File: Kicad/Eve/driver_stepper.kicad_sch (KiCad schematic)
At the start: 16 parts

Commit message: Kicad changes
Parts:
- removed C201, C202, C209: 0603/100nF/50V, symbol Device:C_Small
- removed C203, C204, C205, C207: 150µF/80V/45 mOhm, symbol Device:C_Polarized
- removed C206, C208, C210: 0603/100nF/16V, symbol Device:C_Small
- removed D201: SMBJ54A, symbol Device:D_Schottky
- removed Q? (x4): SQJ504EP-T1_GE3, SQJ968EPT1GE3, symbol SQJ504EP-T1_GE3:SQJ504EP-T1_GE3
- removed U?: TMC2590-TA, TQFP32_7X7_TRI, symbol TMC2590:TMC2590-TA
- added C? (x3): 0603/100nF/50V, symbol Device:C_Small
- added C? (x4): 150µF/80V/45 mOhm, symbol Device:C_Polarized
- added C? (x3): 0603/100nF/16V, symbol Device:C_Small
- added D?: SMBJ54A, symbol Device:D_Schottky
- added J? (x2): Conn_01x03, symbol Connector_Generic:Conn_01x03
- added Q? (x4): SQJ504EP-T1_GE3, SQJ968EPT1GE3, symbol SQJ504EP-T1_GE3:SQJ504EP-T1_GE3
- added R? (x2): 10, symbol Device:R
- added R? (x2): 0.075/2W, symbol Device:R
- added U?: TMC2590-TA, TQFP32_7X7_TRI, symbol TMC2590:TMC2590-TA
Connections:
- net 5VOUT: now also C?.2, U?.9 (5VOUT)
- net A1: now also Q?.5 (D1), Q?.6 (D2), U?.5 (BMA1)
- net A2: now also Q?.5 (D1), Q?.6 (D2), U?.4 (BMA2)
- net B1: now also Q?.5 (D1), Q?.6 (D2), U?.20 (BMB1)
- net B2: now also Q?.5 (D1), Q?.6 (D2), U?.21 (BMB2)
- net CLK: now also U?.16 (CLK)
- net CSN: now also U?.14 (CSN)
- net DIR: now also J?.2 (Pin_2), U?.30 (DIR)
- net ENN: now also U?.15 (ENN)
- net GND: now also C?.1, C?.1, C?.2, C?.2, C?.2, C?.2, C?.2, C?.2, C?.2, D?.2 (A), R?.2, R?.2, U?.1 (GND), U?.13 (SRBL), U?.28 (SRAL), U?.32 (TST_MODE), U?.33 (GND)
- net HA1: now also Q?.4 (G2), U?.2 (HA1)
- net HA2: now also Q?.4 (G2), U?.3 (HA2)
- net HB1: now also Q?.4 (G2), U?.23 (HB1)
- net HB2: now also Q?.4 (G2), U?.22 (HB2)
- net LA1: now also Q?.2 (G1), U?.6 (LA1)
- net LA2: now also Q?.2 (G1), U?.7 (LA2)
- net LB1: now also Q?.2 (G1), U?.19 (LB1)
- net LB2: now also Q?.2 (G1), U?.18 (LB2)
- net MISO: now also U?.10 (SDO)
- net MOSI: now also U?.11 (SDI)
- net SCK: now also U?.12 (SCK)
- net SG_TST: now also U?.27 (SG_TST)
- net SRA: now also R?.2, U?.8 (SRA)
- net SRB: now also R?.2, U?.17 (SRB)
- net STANDALONE_MODE: now also U?.26 (ST_ALONE)
- net STEP: now also J?.2 (Pin_2), U?.31 (STEP)
- net VCC_IO: now also C?.1, U?.29 (VCC_IO)
- net VHS: now also C?.2, U?.24 (VHS)
- new net: Q?.1 (S1), Q?.1 (S1), R?.1, R?.1 (x2)
- new net CON_DIR: J?.3 (Pin_3)
- new net CON_STEP: J?.3 (Pin_3)
- new net EXT_DIR: J?.1 (Pin_1)
- new net EXT_STEP: J?.1 (Pin_1)
- new net Vdc: C?.1, C?.1, C?.1, C?.1, C?.1, C?.1, C?.1, C?.2, D?.1 (K), Q?.3 (S2), Q?.3 (S2), Q?.3 (S2), Q?.3 (S2), U?.25 (VS)

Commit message: updtated Kicad ver 7.11.23
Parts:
- removed J? (x2): Conn_01x03, symbol Connector_Generic:Conn_01x03
- removed Q?: SQJ504EP-T1_GE3, SQJ968EPT1GE3, symbol SQJ504EP-T1_GE3:SQJ504EP-T1_GE3
- added J8: Conn_01x04, symbol Connector_Generic:Conn_01x04
- added Q1: SQJ504EP-T1_GE3, SQJ968EPT1GE3, symbol SQJ504EP-T1_GE3:SQJ504EP-T1_GE3
- C28: renamed from C?; value 150µF/80V/45 mOhm -> 150u; Vmax (none) -> 80
- gave numbers to parts that had none: 18
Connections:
- net A1: now also J8.3 (Pin_3), Q1.5 (D1), Q1.6 (D2)
- net A2: now also J8.4 (Pin_4)
- net B1: now also J8.1 (Pin_1)
- net B2: now also J8.2 (Pin_2)
- net HA1: now also Q1.4 (G2)
- net LA1: now also Q1.2 (G1)
- net Vdc: now also Q1.3 (S2)
- net at Q7.1 (S1), R24.1, R26.1: now also Q1.1 (S1)
- net MISO renamed SDO
- net MOSI renamed SDI

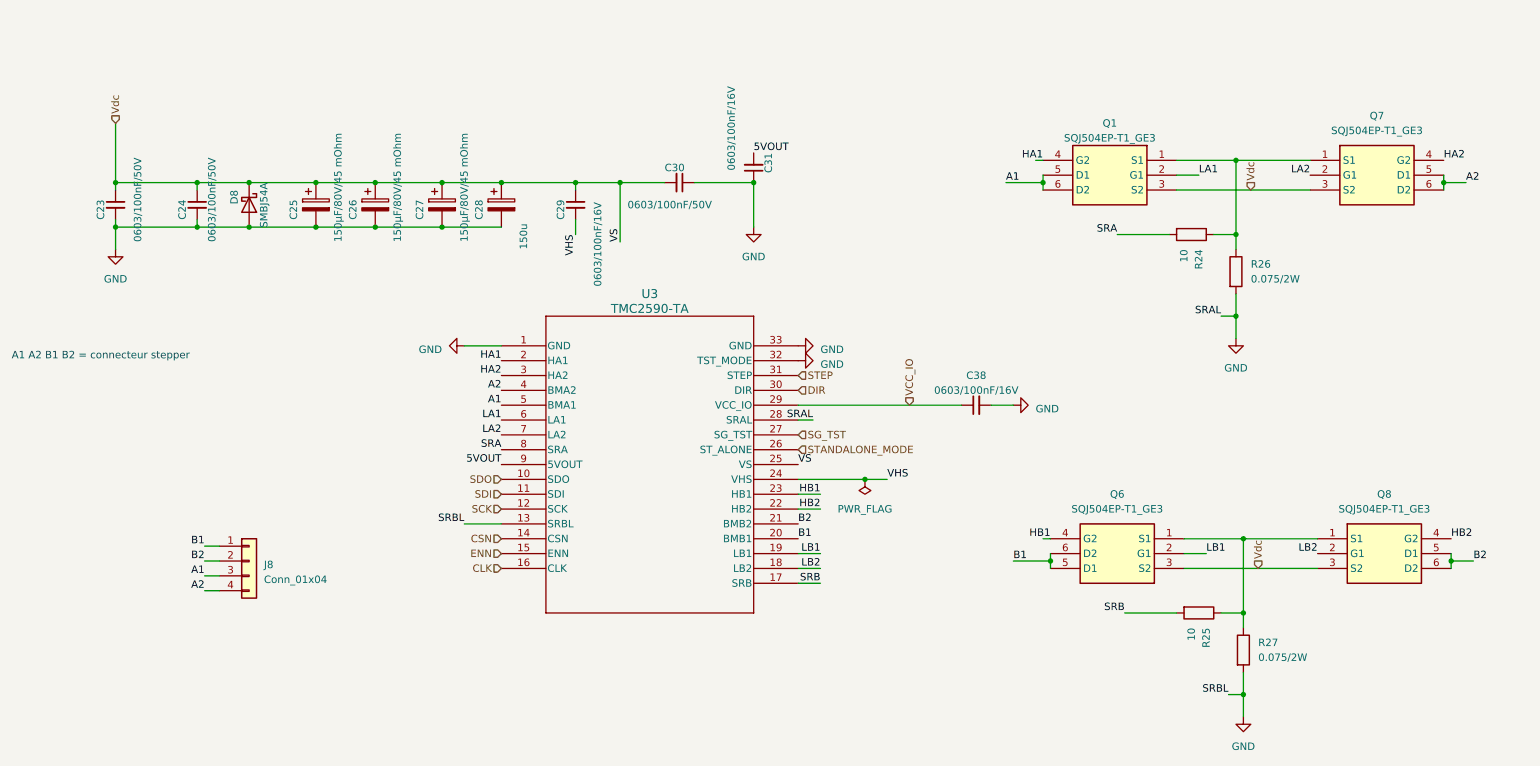
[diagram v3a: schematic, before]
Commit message: added Kicad libraries to git + sch changes 11/11/23
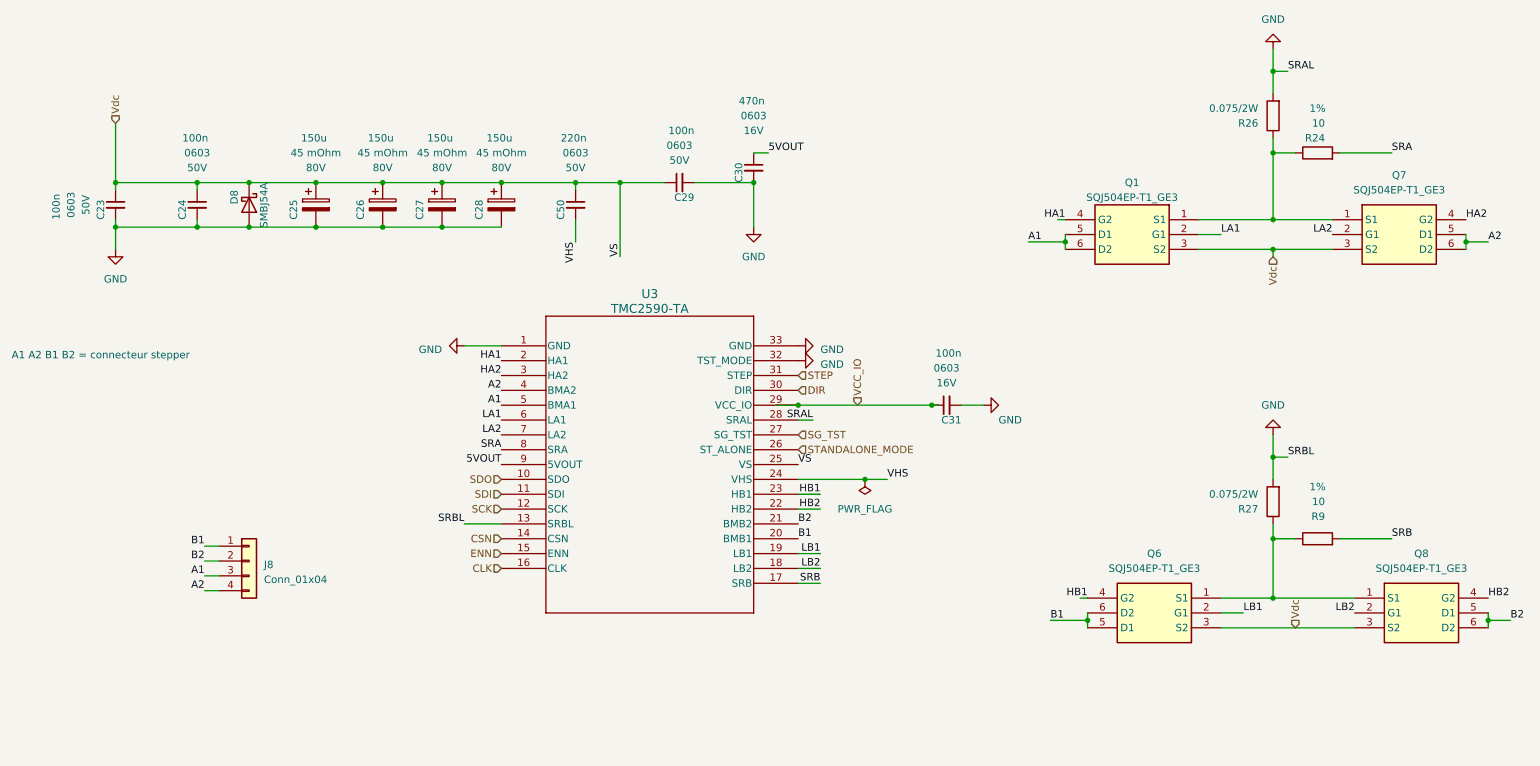
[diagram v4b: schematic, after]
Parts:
- removed C38: 0603/100nF/16V, symbol Device:C_Small
- removed R25: 10, symbol Device:R
- added C50: 220n, symbol Device:C_Small
- added R9: 10, symbol Device:R
- C23, C24: value 0603/100nF/50V -> 100n; Model (none) -> 0603; Voltage (none) -> 50V
- C25, C26, C27: value 150µF/80V/45 mOhm -> 150u; R (none) -> 45 mOhm; Voltage (none) -> 80V
- C28: R (none) -> 45 mOhm; Vmax 80 -> (none); Voltage (none) -> 80V
- C29: value 0603/100nF/16V -> 100n; Model (none) -> 0603; Voltage (none) -> 50V
- C30: value 0603/100nF/50V -> 470n; Model (none) -> 0603; Voltage (none) -> 16V
- C31: value 0603/100nF/16V -> 100n; Model (none) -> 0603; Voltage (none) -> 16V
- R24: Tolerance (none) -> 1%
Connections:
- net 5VOUT: now also C30.1; no longer C31.2
- net GND: now also C29.2, C30.2, C31.2; no longer C30.1, C31.1
- net SRB: now also R9.2
- net VCC_IO: now also C31.1
- net VHS: now also C50.2; no longer C29.2
- net Vdc: now also C50.1; no longer C30.2
- net at Q6.1 (S1), Q8.1 (S1), R27.1: now also R9.1
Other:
- moved on the sheet: Q1, Q6, Q7, Q8, R24, R26, R27
